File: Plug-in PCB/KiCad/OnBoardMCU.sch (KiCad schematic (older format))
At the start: 31 parts, among them J10 Conn_01x01, J11 Conn_01x01, J12 Conn_01x01, J13 Conn_01x01, J14 Conn_01x01, J16 Conn_01x01, J17 Conn_01x01, J3 Conn_01x01, J9 Conn_01x05, U4 ATSAME70N21A-CN, Y1 ABM8G-12.000MHZ-4Y-T3

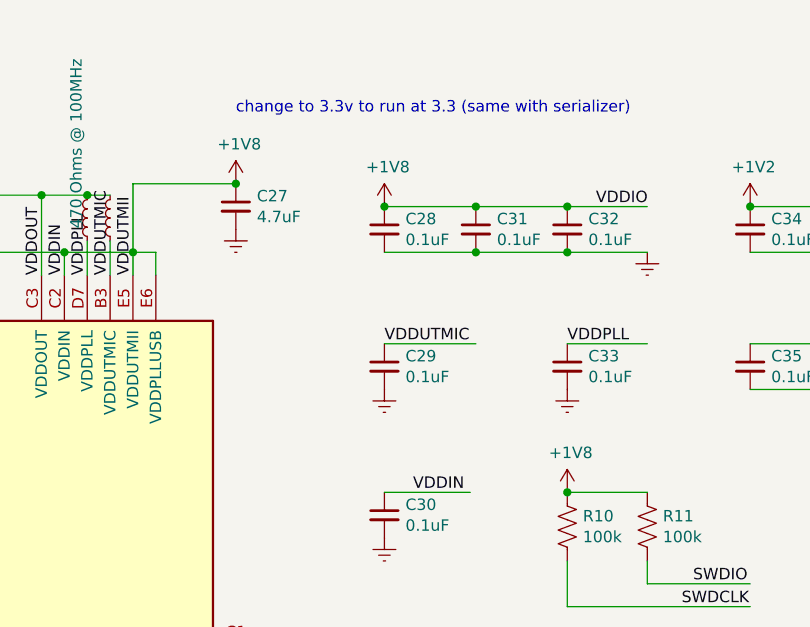
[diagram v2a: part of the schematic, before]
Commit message: Change MCU and Serializer Power to 3.3V
1. MCU VDDIO, SWD, VDDIN, VDDUTMII powered at 3.3V

2. Serializer VDDIO, PDB powered at 3.3V

3. Layout changed (Pins enlarged, Coax_Gnd added, Coax connector moved closer to seralizer)
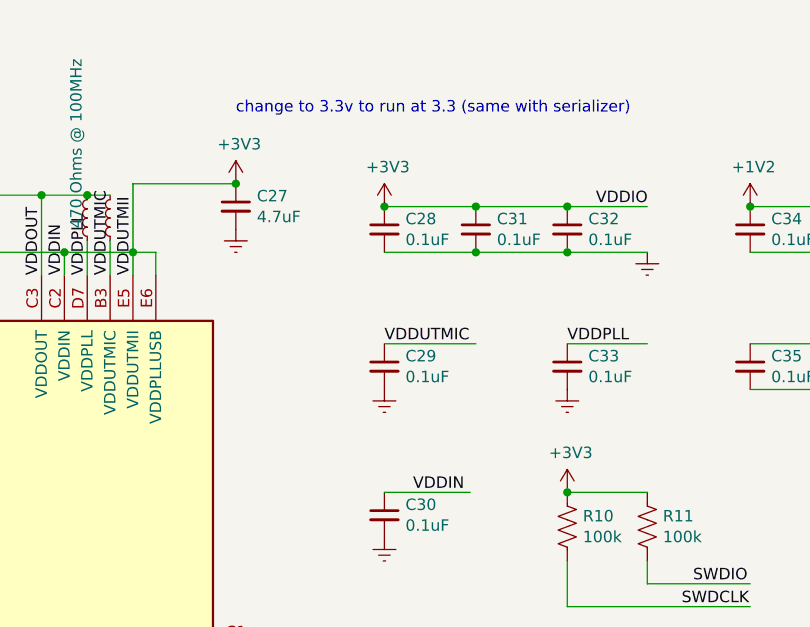
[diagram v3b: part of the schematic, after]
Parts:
- J10, J11, J12, J13, J16, J17, J3: footprint Connector_PinHeader_1.27mm:PinHeader_1x01_P1.27mm_Vertical -> Connector_PinHeader_2.54mm:PinHeader_1x01_P2.54mm_Vertical
- J9: footprint Connector_PinHeader_1.27mm:PinHeader_1x05_P1.27mm_Vertical -> Connector_PinHeader_2.54mm:PinHeader_1x05_P2.54mm_Vertical
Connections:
- net labels added: +3V3
- net labels removed: +1V8
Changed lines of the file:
@@
 	5450 950  5450 1050
 Connection ~ 5900 950
-$Comp
-L power:+1V8 #PWR057
-U 1 1 5C96C772
-P 6650 650
-F 0 "#PWR057" H 6650 500 50  0001 C CNN
-F 1 "+1V8" H 6665 823 50  0000 C CNN
-F 2 "" H 6650 650 50  0001 C CNN
-F 3 "" H 6650 650 50  0001 C CNN
-	1    6650 650
-	1    0    0    -1
-$EndComp
 Wire Wire Line
 	6100 900  6100 1050
@@
 Connection ~ 4950 700
 $Comp
-L power:+1V8 #PWR059
-U 1 1 5CC27956
-P 7300 750
-F 0 "#PWR059" H 7300 600 50  0001 C CNN
-F 1 "+1V8" H 7315 923 50  0000 C CNN
-F 2 "" H 7300 750 50  0001 C CNN
-F 3 "" H 7300 750 50  0001 C CNN
-	1    7300 750
-	1    0    0    -1
-$EndComp
-$Comp
 L .Capacitor:GCJ188R71E104KA12D C28
 U 1 1 5CC27957
@@
 Wire Wire Line
 	7300 750  7700 750
-Connection ~ 7300 750
 Connection ~ 7700 750
 Wire Wire Line
@@
 VDDCORE
 $Comp
-L power:+1V8 #PWR064
-U 1 1 5C9DCFA8
-P 8100 2000
-F 0 "#PWR064" H 8100 1850 50  0001 C CNN
-F 1 "+1V8" H 8115 2173 50  0000 C CNN
-F 2 "" H 8100 2000 50  0001 C CNN
-F 3 "" H 8100 2000 50  0001 C CNN
-	1    8100 2000
-	1    0    0    -1
-$EndComp
-$Comp
 L Device:R_US R10
 U 1 1 5C9DD128
@@
 Wire Wire Line
 	8100 2000 8450 2000
-Connection ~ 8100 2000
 $Comp
 L Device:R_US R11
@@
 	1    0    0    -1
 $EndComp
-Connection ~ 6650 650
 $Comp
 L power:Earth #PWR058
@@
 F 0 "J9" H 9530 4942 50  0000 L CNN
 F 1 "Conn_01x05" H 9530 4851 50  0000 L CNN
-F 2 "Connector_PinHeader_1.27mm:PinHeader_1x05_P1.27mm_Vertical" H 9450 4900 50  0001 C CNN
+F 2 "Connector_PinHeader_2.54mm:PinHeader_1x05_P2.54mm_Vertical" H 9450 4900 50  0001 C CNN
 F 3 "~" H 9450 4900 50  0001 C CNN
 	1    9450 4900
@@
 F 0 "J11" H 1318 5000 50  0000 C CNN
 F 1 "Conn_01x01" H 1318 5091 50  0000 C CNN
-F 2 "Connector_PinHeader_1.27mm:PinHeader_1x01_P1.27mm_Vertical" H 1400 5225 50  0001 C CNN
+F 2 "Connector_PinHeader_2.54mm:PinHeader_1x01_P2.54mm_Vertical" H 1400 5225 50  0001 C CNN
 F 3 "~" H 1400 5225 50  0001 C CNN
 	1    1400 5225
@@
 F 0 "J10" H 1318 4900 50  0000 C CNN
 F 1 "Conn_01x01" H 1318 4991 50  0000 C CNN
-F 2 "Connector_PinHeader_1.27mm:PinHeader_1x01_P1.27mm_Vertical" H 1400 5125 50  0001 C CNN
+F 2 "Connector_PinHeader_2.54mm:PinHeader_1x01_P2.54mm_Vertical" H 1400 5125 50  0001 C CNN
 F 3 "~" H 1400 5125 50  0001 C CNN
 	1    1400 5125
@@
 F 0 "J12" H 8980 3892 50  0000 L CNN
 F 1 "Conn_01x01" H 8980 3801 50  0000 L CNN
-F 2 "Connector_PinHeader_1.27mm:PinHeader_1x01_P1.27mm_Vertical" H 8900 3850 50  0001 C CNN
+F 2 "Connector_PinHeader_2.54mm:PinHeader_1x01_P2.54mm_Vertical" H 8900 3850 50  0001 C CNN
 F 3 "~" H 8900 3850 50  0001 C CNN
 	1    8900 3850
@@
 F 0 "J13" H 8980 3992 50  0000 L CNN
 F 1 "Conn_01x01" H 8980 3901 50  0000 L CNN
-F 2 "Connector_PinHeader_1.27mm:PinHeader_1x01_P1.27mm_Vertical" H 8900 3950 50  0001 C CNN
+F 2 "Connector_PinHeader_2.54mm:PinHeader_1x01_P2.54mm_Vertical" H 8900 3950 50  0001 C CNN
 F 3 "~" H 8900 3950 50  0001 C CNN
 	1    8900 3950
@@
 F 0 "J16" H 8980 4092 50  0000 L CNN
 F 1 "Conn_01x01" H 8980 4001 50  0000 L CNN
-F 2 "Connector_PinHeader_1.27mm:PinHeader_1x01_P1.27mm_Vertical" H 8900 4050 50  0001 C CNN
+F 2 "Connector_PinHeader_2.54mm:PinHeader_1x01_P2.54mm_Vertical" H 8900 4050 50  0001 C CNN
 F 3 "~" H 8900 4050 50  0001 C CNN
 	1    8900 4050
@@
 F 0 "J17" H 8980 4192 50  0000 L CNN
 F 1 "Conn_01x01" H 8980 4101 50  0000 L CNN
-F 2 "Connector_PinHeader_1.27mm:PinHeader_1x01_P1.27mm_Vertical" H 8900 4150 50  0001 C CNN
+F 2 "Connector_PinHeader_2.54mm:PinHeader_1x01_P2.54mm_Vertical" H 8900 4150 50  0001 C CNN
 F 3 "~" H 8900 4150 50  0001 C CNN
 	1    8900 4150
@@
 F 0 "J3" H 1293 2425 50  0000 C CNN
 F 1 "Conn_01x01" H 1293 2516 50  0000 C CNN
-F 2 "Connector_PinHeader_1.27mm:PinHeader_1x01_P1.27mm_Vertical" H 1375 2650 50  0001 C CNN
+F 2 "Connector_PinHeader_2.54mm:PinHeader_1x01_P2.54mm_Vertical" H 1375 2650 50  0001 C CNN
 F 3 "~" H 1375 2650 50  0001 C CNN
 	1    1375 2650
@@
 Wire Wire Line
 	1575 2650 1900 2650
+Text Label 3800 2750 0    50   ~ 0
+WXB_CLK
+Text Label 3550 4950 0    50   ~ 0
+SDA
+Text Label 3550 5050 0    50   ~ 0
+SCL
 Wire Bus Line
 	3100 1650 3100 1850
@@
 Wire Bus Line
 	7600 3950 7600 4300
-Text Label 3800 2750 0    50   ~ 0
-WXB_CLK
-Text Label 3550 4950 0    50   ~ 0
-SDA
-Text Label 3550 5050 0    50   ~ 0
-SCL
+$Comp
+L power:+3V3 #PWR0126
+U 1 1 5D664F4C
+P 6650 650
+F 0 "#PWR0126" H 6650 500 50  0001 C CNN
+F 1 "+3V3" H 6665 823 50  0000 C CNN
+F 2 "" H 6650 650 50  0001 C CNN
+F 3 "" H 6650 650 50  0001 C CNN
+	1    6650 650
+	1    0    0    -1
+$EndComp
+Connection ~ 6650 650
+$Comp
+L power:+3V3 #PWR0127
+U 1 1 5D68A0EF
+P 7300 750
+F 0 "#PWR0127" H 7300 600 50  0001 C CNN
+F 1 "+3V3" H 7315 923 50  0000 C CNN
+F 2 "" H 7300 750 50  0001 C CNN
+F 3 "" H 7300 750 50  0001 C CNN
+	1    7300 750
+	1    0    0    -1
+$EndComp
+Connection ~ 7300 750
+$Comp
+L power:+3V3 #PWR0129
+U 1 1 5D68E764
+P 8100 2000
+F 0 "#PWR0129" H 8100 1850 50  0001 C CNN
+F 1 "+3V3" H 8115 2173 50  0000 C CNN
+F 2 "" H 8100 2000 50  0001 C CNN
+F 3 "" H 8100 2000 50  0001 C CNN
+	1    8100 2000
+	1    0    0    -1
+$EndComp
+Connection ~ 8100 2000
 $EndSCHEMATC
